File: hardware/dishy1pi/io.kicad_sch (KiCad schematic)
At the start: 30 parts, among them CN2 KF2EDGR-2.54-9P, CN3 KF2EDGR-2.54-6P, U2 LTV-847S, U3 LTV-827S-TA1, U4 LTV-817S-TA1, U5 LTV-817S-TA1

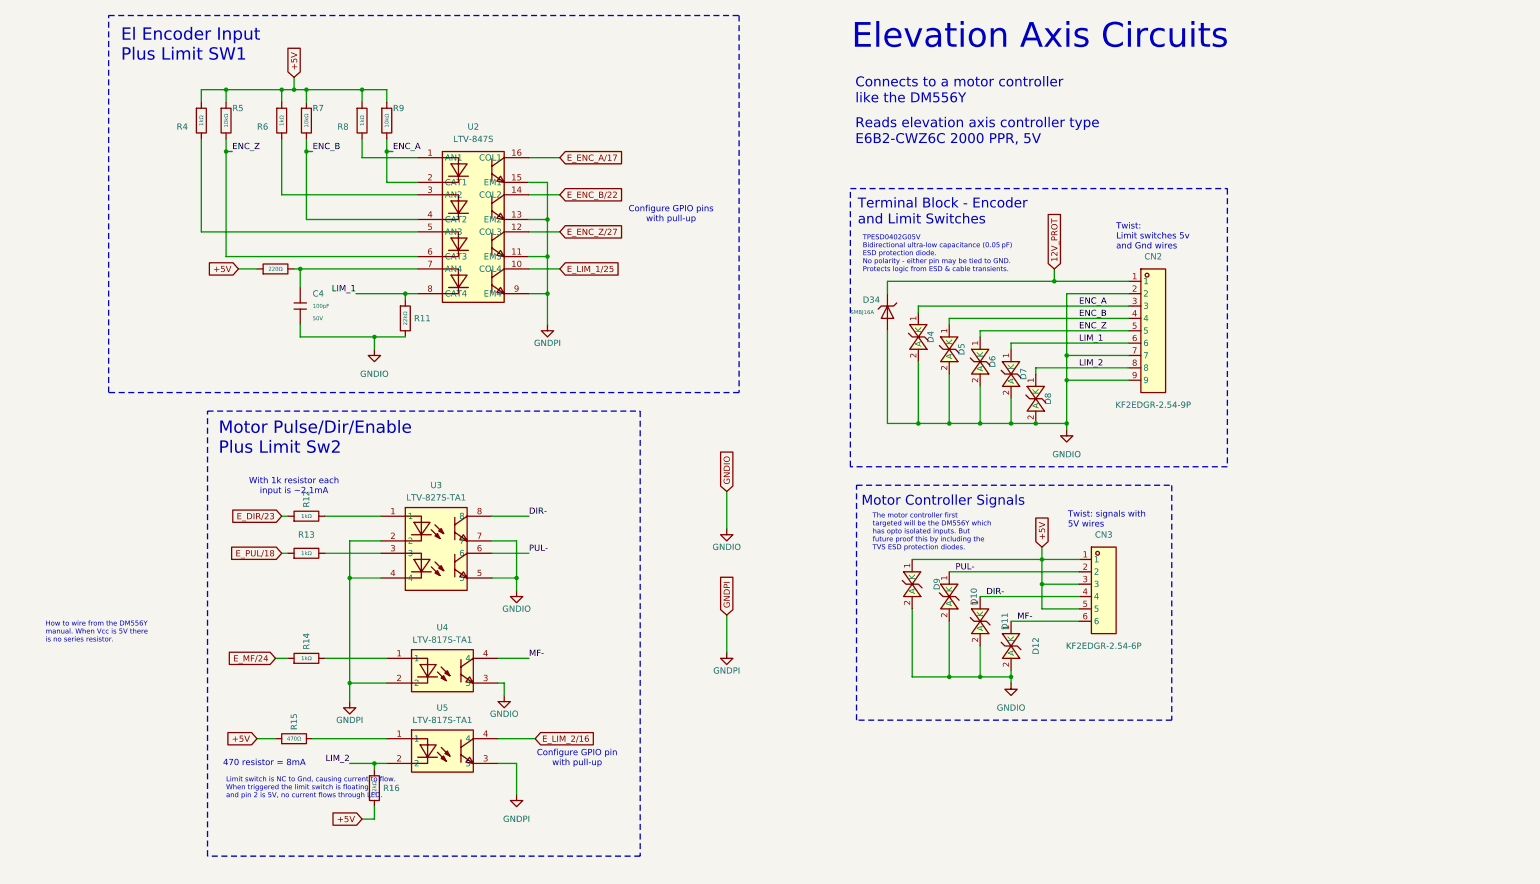
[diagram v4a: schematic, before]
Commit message: Added 12V power input
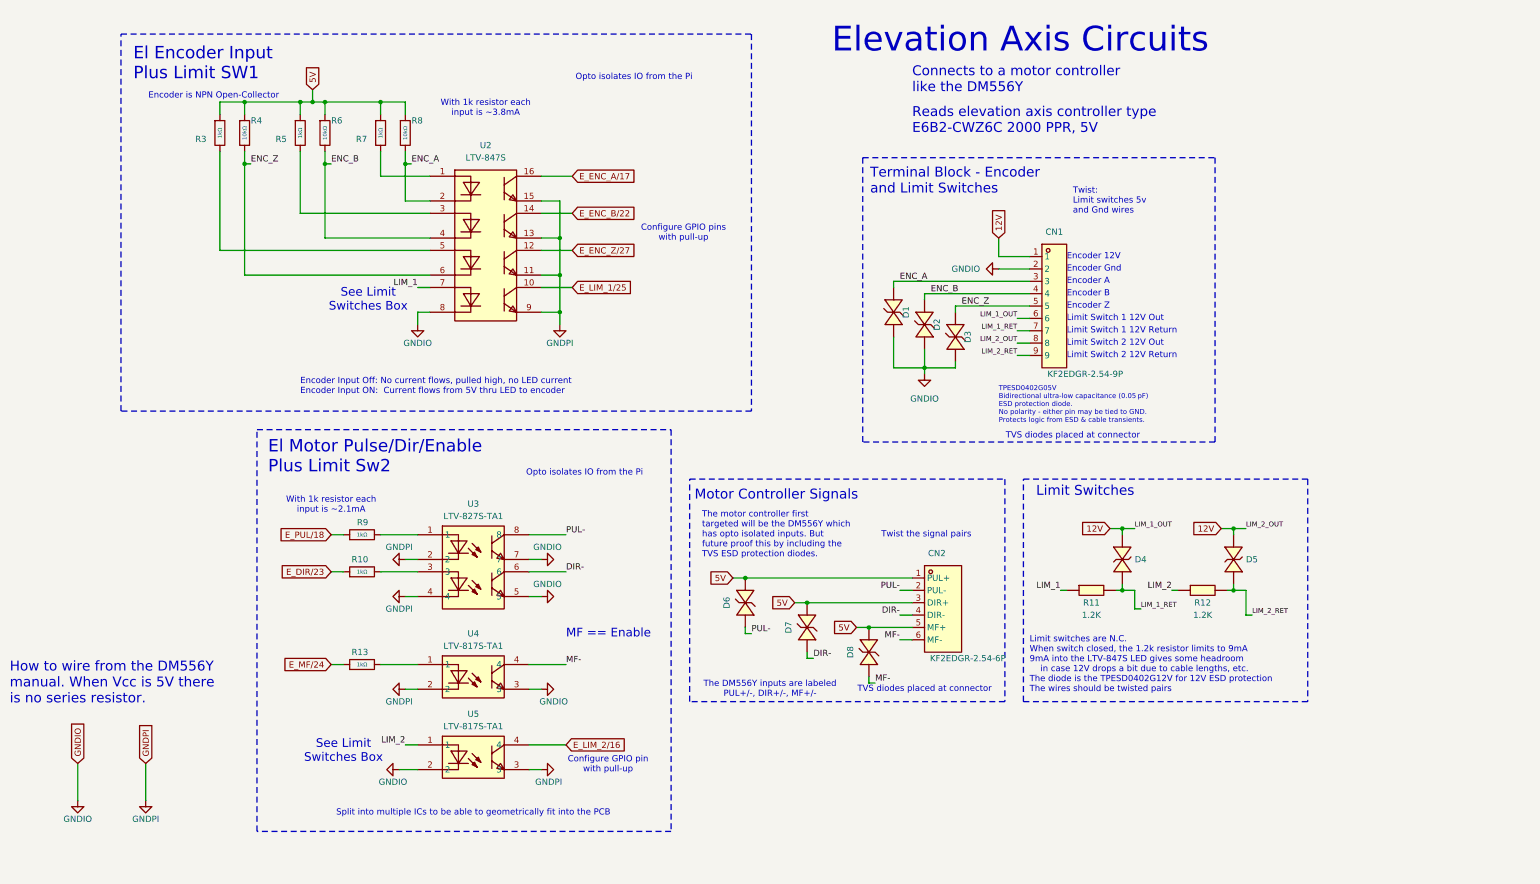
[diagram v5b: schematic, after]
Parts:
- removed C4: 100pF, PCM_JLCPCB:C_0402, symbol PCM_JLCPCB-Capacitors:0402,100pF
- removed CN2: KF2EDGR-2.54-9P, MyParts:CONN-TH_9P-P2.54_KF2EDGR-2.54-9P, symbol MyParts:KF2EDGR-2.54-9P
- removed CN3: KF2EDGR-2.54-6P, MyParts:CONN-TH_KF2EDGR-2.54-6P, symbol MyParts:KF2EDGR-2.54-6P
- removed D10, D11, D12, D4, D5, D9: TPESD0402G05V, MyParts:D0402-BI, symbol MyParts:TPESD0402G05V
- removed D34: SMBJ16A, PCM_JLCPCB:D_SMB, symbol PCM_JLCPCB-Diodes:TVS-Uni,SMBJ16A
- removed R10: 220Ω, PCM_JLCPCB:R_0402, symbol PCM_JLCPCB-Resistors:0402,220Ω
- removed R11, R16: 22kΩ, PCM_JLCPCB:R_0402, symbol PCM_JLCPCB-Resistors:0402,22kΩ
- removed R12, R14, R4, R6, R8: 1kΩ, PCM_JLCPCB:R_0402, symbol PCM_JLCPCB-Resistors:0402,1kΩ
- removed R15: 470Ω, PCM_JLCPCB:R_0402, symbol PCM_JLCPCB-Resistors:0402,470Ω
- removed R5, R7, R9: 10kΩ, PCM_JLCPCB:R_0402, symbol PCM_JLCPCB-Resistors:0402,10kΩ
- added CN1: KF2EDGR-2.54-9P, MyParts:CONN-TH_9P-P2.54_KF2EDGR-2.54-9P, symbol MyParts:KF2EDGR-2.54-9P
- added CN2: KF2EDGR-2.54-6P, MyParts:CONN-TH_KF2EDGR-2.54-6P, symbol MyParts:KF2EDGR-2.54-6P
- added D1, D2, D3: TPESD0402G05V, MyParts:D0402-BI, symbol MyParts:TPESD0402G05V
- added D4, D5: TPESD0402G12V, MyParts:D0402-BI, symbol MyParts:TPESD0402G12V
- added R10, R3, R5, R7, R9: 1kΩ, PCM_JLCPCB:R_0402, symbol PCM_JLCPCB-Resistors:0402,1kΩ
- added R11, R12: 1.2K, MyParts:R1206, symbol MyParts:1206W4F1201T5E
- added R4, R6, R8: 10kΩ, PCM_JLCPCB:R_0402, symbol PCM_JLCPCB-Resistors:0402,10kΩ
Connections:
- net DIR-: now also D7.2 (A), U3.6, CN2.4 (DIR-); no longer U3.8
- net ENC_A: now also CN1.3, D1.1 (K), R8.2
- net ENC_B: now also CN1.4, D2.1 (K), R6.2
- net ENC_Z: now also CN1.5, D3.1 (K), R4.2; no longer D6.1 (K)
- net E_DIR/23: now also R10.1
- net E_MF/24: now also R13.1
- net E_PUL/18: now also R9.1; no longer R13.1
- net GNDIO: now also U2.8 (CAT4), U5.2, CN1.2, D1.2 (A), D2.2 (A), D3.2 (A); no longer D6.2 (A), D7.2 (A), D8.2 (A)
- net LIM_1: now also U2.7 (AN4), R11.1; no longer D7.1 (K), U2.8 (CAT4)
- net LIM_2: now also U5.1, R12.1; no longer D8.1 (K), U5.2
- net MF-: now also D8.2 (A), CN2.6 (MF-)
- net PUL-: now also D6.2 (A), U3.8, CN2.2 (PUL-); no longer U3.6
- net at U4.1: now also R13.2
- net at U2.5 (AN3): now also R3.2
- net at U2.1 (AN1): now also R7.2
- net at U2.3 (AN2): now also R5.2
- net at U3.1: now also R9.2
- net at U3.3: now also R10.2; no longer R13.2
- new net 12V: CN1.1, CN1.6, CN1.8, D4.1, D5.1
- new net 5V: CN2.1 (PUL+), CN2.3 (DIR+), CN2.5 (MF+), D6.1 (K), D7.1 (K), D8.1 (K), R3.1, R4.1, R5.1, R6.1, R7.1, R8.1
- new net LIM_1_RET: CN1.7, D4.2, R11.2
- new net LIM_2_RET: CN1.9, D5.2, R12.2
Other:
- note added: "El Motor Pulse/Dir/Enable Plus Limit Sw2"
- note added: "Encoder 12V"
- note added: "Encoder A"
- note added: "Encoder B"
- note added: "Encoder Gnd"
- note added: "Encoder Input Off: No current flows, pulled high, no LED current Encoder Input ON: Current flows from 5V thru LED to encoder"
- note added: "Encoder Z"
- note added: "Encoder is NPN Open-Collector"
- note added: "Limit Switch 1 12V Out"
- note added: "Limit Switch 1 12V Return"
- note added: "Limit Switch 2 12V Out"
- note added: "Limit Switch 2 12V Return"
- note added: "Limit Switches"
- note added: "Limit switches are N.C. When switch closed, the 1.2k resistor limits to 9mA 9mA into the LTV-847S LED gives some headroom in case 12V drops a bit due to cable lengths, etc. The diode is the TPESD0402G12V for 12V ESD protection The wires should be twisted pairs"
- note added: "MF == Enable"
- note added: "Opto isolates IO from the Pi"
- note added: "See Limit Switches Box"
- note added: "Split into multiple ICs to be able to geometrically fit into the PCB"
- note added: "TVS diodes placed at connector"
- note added: "The DM556Y inputs are labeled PUL+/-, DIR+/-, MF+/-"
- note added: "Twist the signal pairs"
- note added: "With 1k resistor each input is ~3.8mA"
- note removed: "470 resistor = 8mA"
- note removed: "Limit switch is NC to Gnd, causing current to flow. When triggered the limit switch is floating and pin 2 is 5V, no current flows through LED."
- note removed: "Motor Pulse/Dir/Enable Plus Limit Sw2"
- note removed: "Twist: signals with 5V wires"

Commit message: Pushed latest parts lib
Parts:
- removed R12: 1.2K, MyParts:R1206, symbol MyParts:1206W4F1201T5E
- added R38: 1.2K, MyParts:C0603, symbol MyParts:1206W4F1201T5E
- R11: footprint MyParts:R1206 -> MyParts:C0603
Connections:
- net LIM_1: now also R38.1; no longer R11.1
- net LIM_1_RET: now also R38.2; no longer R11.2
- net LIM_2: now also R11.1
- net LIM_2_RET: now also R11.2
- net E_DIR/23 renamed EL_DIR_MCU
- net E_ENC_A/17 renamed EL_ENC_A_MCU
- net E_ENC_B/22 renamed EL_ENC_B_MCU
- net E_ENC_Z/27 renamed EL_ENC_Z_MCU
- net E_LIM_1/25 renamed EL_LIM_1_MCU
- net E_LIM_2/16 renamed EL_LIM_2_MCU
- net E_MF/24 renamed EL_ENABLE_MCU
- net E_PUL/18 renamed EL_PUL_MCU
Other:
- moved on the sheet: CN2
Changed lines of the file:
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@@
 		)
 	)
-	(global_label "E_LIM_1{slash}25"
+	(global_label "EL_LIM_1_MCU"
 		(shape input)
 		(at 133.35 72.39 0)
@@
 		)
 		(property "Intersheetrefs" "${INTERSHEET_REFS}"
-			(at 147.5578 72.39 0)
+			(at 149.8559 72.39 0)
 			(effects
 				(font
@@
 		)
 	)
-	(global_label "E_ENC_B{slash}22"
+	(global_label "EL_ENC_B_MCU"
 		(shape input)
 		(at 133.35 57.15 0)
@@
 		)
 		(property "Intersheetrefs" "${INTERSHEET_REFS}"
-			(at 148.2835 57.15 0)
+			(at 150.5816 57.15 0)
 			(effects
 				(font
@@
 		)
 	)
-	(global_label "E_MF{slash}24"
+	(global_label "EL_ENABLE_MCU"
 		(shape input)
 		(at 83.82 149.86 180)
@@
 		)
 		(property "Intersheetrefs" "${INTERSHEET_REFS}"
-			(at 72.3336 149.86 0)
+			(at 65.5603 149.86 0)
 			(effects
 				(font
@@
 		)
 	)
-	(global_label "E_PUL{slash}18"
+	(global_label "EL_PUL_MCU"
 		(shape input)
 		(at 83.82 123.19 180)
@@
 		)
 		(property "Intersheetrefs" "${INTERSHEET_REFS}"
-			(at 71.245 123.19 0)
+			(at 68.9469 123.19 0)
 			(effects
 				(font
@@
 		)
 	)
-	(global_label "E_ENC_A{slash}17"
+	(global_label "EL_ENC_A_MCU"
 		(shape input)
 		(at 133.35 49.53 0)
@@
 		)
 		(property "Intersheetrefs" "${INTERSHEET_REFS}"
-			(at 148.1021 49.53 0)
+			(at 150.4002 49.53 0)
 			(effects
 				(font
@@
 		)
 	)
-	(global_label "E_LIM_2{slash}16"
+	(global_label "EL_LIM_2_MCU"
 		(shape input)
 		(at 132.08 166.37 0)
@@
 		)
 		(property "Intersheetrefs" "${INTERSHEET_REFS}"
-			(at 146.2878 166.37 0)
+			(at 148.5859 166.37 0)
 			(effects
 				(font
@@
 		)
 	)
-	(global_label "E_DIR{slash}23"
+	(global_label "EL_DIR_MCU"
 		(shape input)
 		(at 83.82 130.81 180)
@@
 		)
 		(property "Intersheetrefs" "${INTERSHEET_REFS}"
-			(at 71.7288 130.81 0)
+			(at 69.4307 130.81 0)
 			(effects
 				(font
@@
 		)
 	)
-	(global_label "E_ENC_Z{slash}27"
+	(global_label "EL_ENC_Z_MCU"
 		(shape input)
 		(at 133.35 64.77 0)
@@
 		)
 		(property "Intersheetrefs" "${INTERSHEET_REFS}"
-			(at 148.223 64.77 0)
+			(at 150.5211 64.77 0)
 			(effects
 				(font
@@
 	)
 	(symbol
-		(lib_name "TPESD0402G05V_3")
 		(lib_id "MyParts:TPESD0402G05V")
 		(at 199.39 77.47 270)
@@
 	)
 	(symbol
-		(lib_id "MyParts:1206W4F1201T5E")
-		(at 262.89 134.62 0)
-		(unit 1)
-		(exclude_from_sim no)
-		(in_bom yes)
-		(on_board yes)
-		(dnp no)
-		(property "Reference" "R12"
-			(at 262.89 137.16 0)
-			(effects
-				(font
-					(size 1.27 1.27)
-				)
-			)
-		)
-		(property "Value" "1.2K"
-			(at 262.89 139.7 0)
-			(effects
-				(font
-					(size 1.27 1.27)
-				)
-			)
-		)
-		(property "Footprint" "MyParts:R1206"
-			(at 262.89 142.24 0)
-			(effects
-				(font
-					(size 1.27 1.27)
-				)
-				(hide yes)
-			)
-		)
-		(property "Datasheet" "https://lcsc.com/product-detail/Chip-Resistor-Surface-Mount-UniOhm_1-2KR-1201-1_C17891.html"
-			(at 262.89 144.78 0)
-			(effects
-				(font
-					(size 1.27 1.27)
-				)
-				(hide yes)
-			)
-		)
-		(property "Description" ""
-			(at 262.89 134.62 0)
-			(effects
-				(font
-					(size 1.27 1.27)
-				)
-				(hide yes)
-			)
-		)
-		(property "LCSC Part" "C17891"
-			(at 262.89 147.32 0)
-			(effects
-				(font
-					(size 1.27 1.27)
-				)
-				(hide yes)
-			)
-		)
-		(pin "2"
-		)
-		(pin "1"
-		)
-		(instances
-			(project "DishyPi1"
-				(path "/e63e39d7-6ac0-4ffd-8aa3-1841a4541b55/d09dd7bf-7813-496f-944b-ba766657ce5d"
-					(reference "R12")
-					(unit 1)
-				)
-			)
-		)
-	)
-	(symbol
 		(lib_id "MyParts:KF2EDGR-2.54-9P")
 		(at 232.41 76.2 0)
@@
 	)
 	(symbol
-		(lib_name "TPESD0402G12V_1")
 		(lib_id "MyParts:TPESD0402G12V")
 		(at 246.38 128.27 270)
@@
 	)
 	(symbol
-		(lib_name "TPESD0402G05V_1")
 		(lib_id "MyParts:TPESD0402G05V")
 		(at 212.09 82.55 270)
@@
 	)
 	(symbol
-		(lib_name "TPESD0402G05V_4")
 		(lib_id "MyParts:TPESD0402G05V")
 		(at 194.31 147.32 270)
@@
 	)
 	(symbol
-		(lib_name "1206W4F1201T5E_1")
-		(lib_id "MyParts:1206W4F1201T5E")
-		(at 240.03 134.62 0)
-		(unit 1)
-		(exclude_from_sim no)
-		(in_bom yes)
-		(on_board yes)
-		(dnp no)
-		(property "Reference" "R11"
-			(at 240.03 137.16 0)
-			(effects
-				(font
-					(size 1.27 1.27)
-				)
-			)
-		)
-		(property "Value" "1.2K"
-			(at 240.03 139.7 0)
-			(effects
-				(font
-					(size 1.27 1.27)
-				)
-			)
-		)
-		(property "Footprint" "MyParts:R1206"
-			(at 240.03 142.24 0)
-			(effects
-				(font
-					(size 1.27 1.27)
-				)
-				(hide yes)
-			)
-		)
-		(property "Datasheet" "https://lcsc.com/product-detail/Chip-Resistor-Surface-Mount-UniOhm_1-2KR-1201-1_C17891.html"
-			(at 240.03 144.78 0)
-			(effects
-				(font
-					(size 1.27 1.27)
-				)
-				(hide yes)
-			)
-		)
-		(property "Description" ""
-			(at 240.03 134.62 0)
-			(effects
-				(font
-					(size 1.27 1.27)
-				)
-				(hide yes)
-			)
-		)
-		(property "LCSC Part" "C17891"
-			(at 240.03 147.32 0)
-			(effects
-				(font
-					(size 1.27 1.27)
-				)
-				(hide yes)
-			)
-		)
-		(pin "2"
-		)
-		(pin "1"
-		)
-		(instances
-			(project "DishyPi1"
-				(path "/e63e39d7-6ac0-4ffd-8aa3-1841a4541b55/d09dd7bf-7813-496f-944b-ba766657ce5d"
-					(reference "R11")
-					(unit 1)
-				)
-			)
-		)
-	)
-	(symbol
 		(lib_id "power:GND")
 		(at 97.79 171.45 270)
@@
 	)
 	(symbol
-		(lib_name "TPESD0402G05V_4")
 		(lib_id "MyParts:TPESD0402G05V")
 		(at 168.91 137.16 270)
@@
 	)
 	(symbol
+		(lib_name "1206W4F1201T5E_1")
+		(lib_id "MyParts:1206W4F1201T5E")
+		(at 262.89 134.62 0)
+		(unit 1)
+		(exclude_from_sim no)
+		(in_bom yes)
+		(on_board yes)
+		(dnp no)
+		(property "Reference" "R11"
+			(at 262.89 137.16 0)
+			(effects
+				(font
+					(size 1.27 1.27)
+				)
+			)
+		)
+		(property "Value" "1.2K"
+			(at 262.89 139.7 0)
+			(effects
+				(font
+					(size 1.27 1.27)
+				)
+				(hide yes)
+			)
+		)
+		(property "Footprint" "MyParts:C0603"
+			(at 262.89 142.24 0)
+			(effects
+				(font
+					(size 1.27 1.27)
+				)
+				(hide yes)
+			)
+		)
+		(property "Datasheet" "https://lcsc.com/product-detail/Chip-Resistor-Surface-Mount-UniOhm_1-2KR-1201-1_C17891.html"
+			(at 262.89 144.78 0)
+			(effects
+				(font
+					(size 1.27 1.27)
+				)
+				(hide yes)
+			)
+		)
+		(property "Description" ""
+			(at 262.89 134.62 0)
+			(effects
+				(font
+					(size 1.27 1.27)
+				)
+				(hide yes)
+			)
+		)
+		(property "LCSC Part" "C17891"
+			(at 262.89 147.32 0)
+			(effects
+				(font
+					(size 1.27 1.27)
+				)
+				(hide yes)
+			)
+		)
+		(pin "2"
+		)
+		(pin "1"
+		)
+		(instances
+			(project "DishyPi1"
+				(path "/e63e39d7-6ac0-4ffd-8aa3-1841a4541b55/d09dd7bf-7813-496f-944b-ba766657ce5d"
+					(reference "R11")
+					(unit 1)
+				)
+			)
+		)
+	)
+	(symbol
 		(lib_id "power:GND")
 		(at 99.06 154.94 270)
@@
 	)
 	(symbol
+		(lib_name "1206W4F1201T5E_1")
+		(lib_id "MyParts:1206W4F1201T5E")
+		(at 240.03 134.62 0)
+		(unit 1)
+		(exclude_from_sim no)
+		(in_bom yes)
+		(on_board yes)
+		(dnp no)
+		(property "Reference" "R38"
+			(at 240.03 137.16 0)
+			(effects
+				(font
+					(size 1.27 1.27)
+				)
+			)
+		)
+		(property "Value" "1.2K"
+			(at 240.03 139.7 0)
+			(effects
+				(font
+					(size 1.27 1.27)
+				)
+			)
+		)
+		(property "Footprint" "MyParts:C0603"
+			(at 240.03 142.24 0)
+			(effects
+				(font
+					(size 1.27 1.27)
+				)
+				(hide yes)
+			)
+		)
+		(property "Datasheet" "https://lcsc.com/product-detail/Chip-Resistor-Surface-Mount-UniOhm_1-2KR-1201-1_C17891.html"
+			(at 240.03 144.78 0)
+			(effects
+				(font
+					(size 1.27 1.27)
+				)
+				(hide yes)
+			)
+		)
+		(property "Description" ""
+			(at 240.03 134.62 0)
+			(effects
+				(font
+					(size 1.27 1.27)
+				)
+				(hide yes)
+			)
+		)
+		(property "LCSC Part" "C17891"
+			(at 240.03 147.32 0)
+			(effects
+				(font
+					(size 1.27 1.27)
+				)
+				(hide yes)
+			)
+		)
+		(pin "2"
+		)
+		(pin "1"
+		)
+		(instances
+			(project "DishyPi1"
+				(path "/e63e39d7-6ac0-4ffd-8aa3-1841a4541b55/d09dd7bf-7813-496f-944b-ba766657ce5d"
+					(reference "R38")
+					(unit 1)
+				)
+			)
+		)
+	)
+	(symbol
 		(lib_id "PCM_JLCPCB-Resistors:0402,1kΩ")
 		(at 93.98 40.64 0)
@@
 	)
 	(symbol
-		(lib_name "TPESD0402G05V_2")
 		(lib_id "MyParts:TPESD0402G05V")
 		(at 205.74 80.01 270)
@@
 	)
 	(symbol
-		(lib_name "TPESD0402G05V_4")
 		(lib_id "MyParts:TPESD0402G05V")
 		(at 181.61 142.24 270)
